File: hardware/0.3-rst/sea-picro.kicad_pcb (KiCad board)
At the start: 4 copper layers, 17.8 x 33 mm, 58 parts, among them J1 USB_C_Receptacle_USB2.0, J2 0.1" x 12, J3 0.1" x 12, J4 D+, J5 D-, Q1 2N7002VC-7, Q2 2N7002VC-7, SW1 SWITCH, U1 AP7365-33WG-7, U2 GD25Q64CWIGR, U3 RP2040, Y1 12MHz

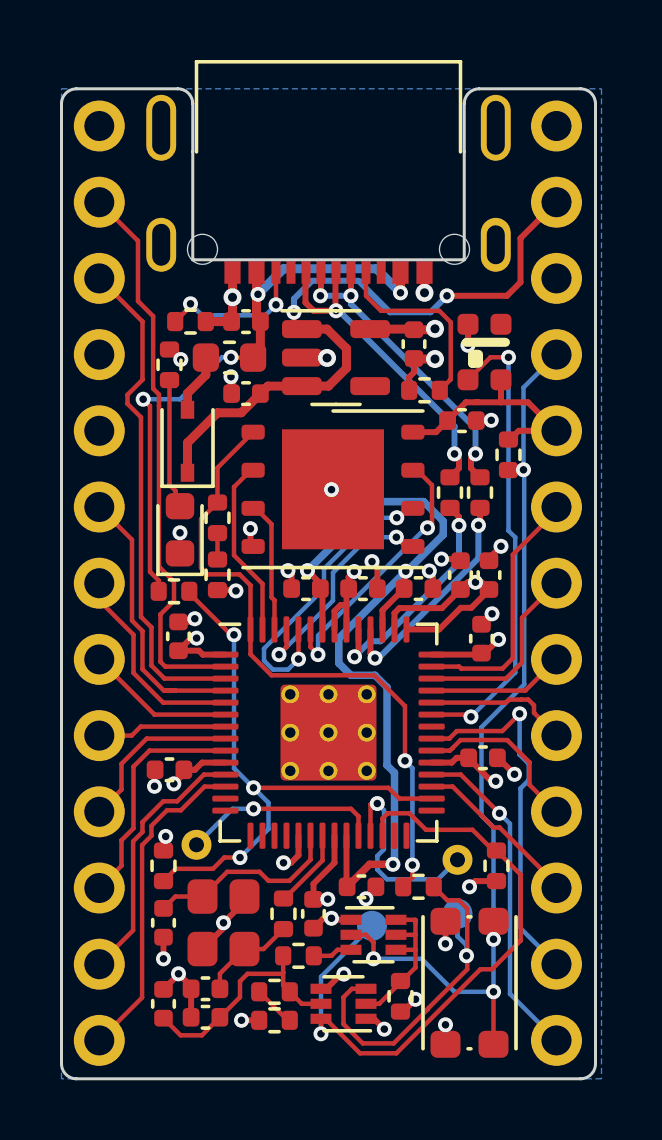
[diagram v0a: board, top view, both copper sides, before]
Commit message: rst moved to new footprints, clean up ext
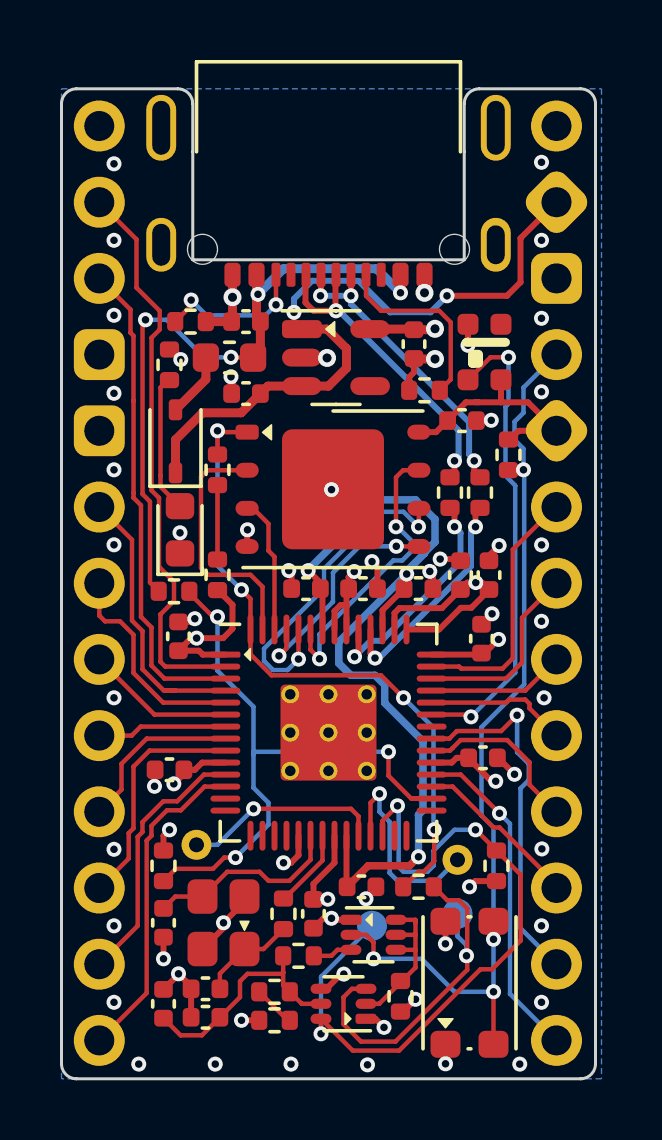
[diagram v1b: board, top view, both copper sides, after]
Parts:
- removed J3: 0.1" x 12, josh-connectors:Castellated_Short_P2.54x12
- removed J4: D+, josh-connectors:PinHeader_1x01_P2.54mm_Circle
- removed J5: D-, josh-connectors:PinHeader_1x01_P2.54mm_Circle
- D1: footprint Diode_SMD:D_SOD-323 -> josh-passives-smt:D_SOD-323
- J2: value 0.1" x 12 -> Sea-Picro; footprint josh-connectors:Castellated_Short_P2.54x12 -> josh-module:Sea-Picro_RST_Pins
- Q1, Q2: footprint Package_TO_SOT_SMD:SOT-563 -> josh-soic-sot-etc:SOT-563
- U1: footprint Package_TO_SOT_SMD:SOT-23-5 -> josh-soic-sot-etc:SOT-23-5
- U2: footprint Package_SON:WSON-8-1EP_6x5mm_P1.27mm_EP3.4x4mm -> josh-dfn-qfn:WSON-8-1EP_6x5mm_P1.27mm_EP3.4x4mm
- moved J2 17.0 mm to (126.1, 91.3), turned to 0 degrees
- moved R10 1.60 mm to (122.5, 87.5)
- moved D1 0.40 mm to (121.1, 86.5)
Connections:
- J2 pad 1: /9 -> /USB+
- J2 pad 10: GND -> /6
- J2 pad 11: /1_RX0 -> /7
- J2 pad 12: /0_TX0 -> /8
- J2 pad 2: /8 -> /0_TX0
- J2 pad 3: /7 -> /1_RX0
- J2 pad 4: /6 -> GND
- J2 pad 5: /5 -> GND
- J2 pad 6: /4 -> /2_SDA1
- J2 pad 8: /2_SDA1 -> /4
- J2 pad 9: GND -> /5
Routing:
- net /nRST: track 21.8 -> 24.5 mm, vias 1 -> 3
- net VBUS: track 20.0 -> 22.6 mm
- net /FLASH_SD1: track 5.92 -> 8.40 mm
- net +3V3: track 36.5 -> 38.6 mm, vias 12 -> 11
- net Net-(R10-Pad1): track 0.88 -> 2.48 mm
- net /VBUS_DETECT: track 19.4 -> 20.9 mm
- net /FLASH_SCK: track 9.86 -> 11.1 mm
- net /FLASH_nCS: track 21.6 -> 22.7 mm, vias 2 -> 4
- net /FLASH_SD3: track 8.88 -> 9.73 mm
- net +1V1: track 27.9 -> 28.6 mm
- net GND: track 28.0 -> 28.2 mm, vias 31 -> 56
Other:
- board text removed: "G"

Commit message: add teardrops and melted versions, update LDO MPN
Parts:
- U1: value AP7365-33WG-7 -> XC6210B332MR-G
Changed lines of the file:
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@@
     (tags "SOT TO_SOT_SMD")
     (property "JLC Basic" "N")
-    (property "LCSC" "C150742")
-    (property "LCSC2" "C82942")
-    (property "MPN " "AP7365-33WG-7 ")
-    (property "MPN2" "ME6211C33M5G-N")
-    (property "Manufacturer" "Diodes Incorporated")
-    (property "Manufacturer2" "MICRONE(Nanjing Micro One Elec) ")
+    (property "LCSC" "C47719")
+    (property "LCSC2" "")
+    (property "MPN " "XC6210B332MR-G")
+    (property "MPN2" "")
+    (property "Manufacturer" "Torex Semiconductor")
+    (property "Manufacturer2" "")
     (property "Sheetfile" "sea-picro.kicad_sch")
     (property "Sheetname" "")
-    (property "Substitute" "Y - Confirm with Josh")
+    (property "Substitute" "N")
     (attr smd)
     (fp_text reference "U1" (at 0 -2.4) (layer "F.SilkS") hide
       (effects (font (size 1 1) (thickness 0.15)))
     )
-    (fp_text value "AP7365-33WG-7 " (at 0 2.4) (layer "F.Fab")
+    (fp_text value "XC6210B332MR-G" (at 0 2.4) (layer "F.Fab")
       (effects (font (size 1 1) (thickness 0.15)))
     )
